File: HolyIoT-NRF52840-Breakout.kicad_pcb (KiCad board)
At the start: 2 copper layers, 45 x 60 mm, 8 parts, among them J1 Conn_01x22_Male, J2 Conn_01x22_Male, J3 Conn_01x11_Male, P1 USB_micro_B, U1 HolyIOT_NRF52840

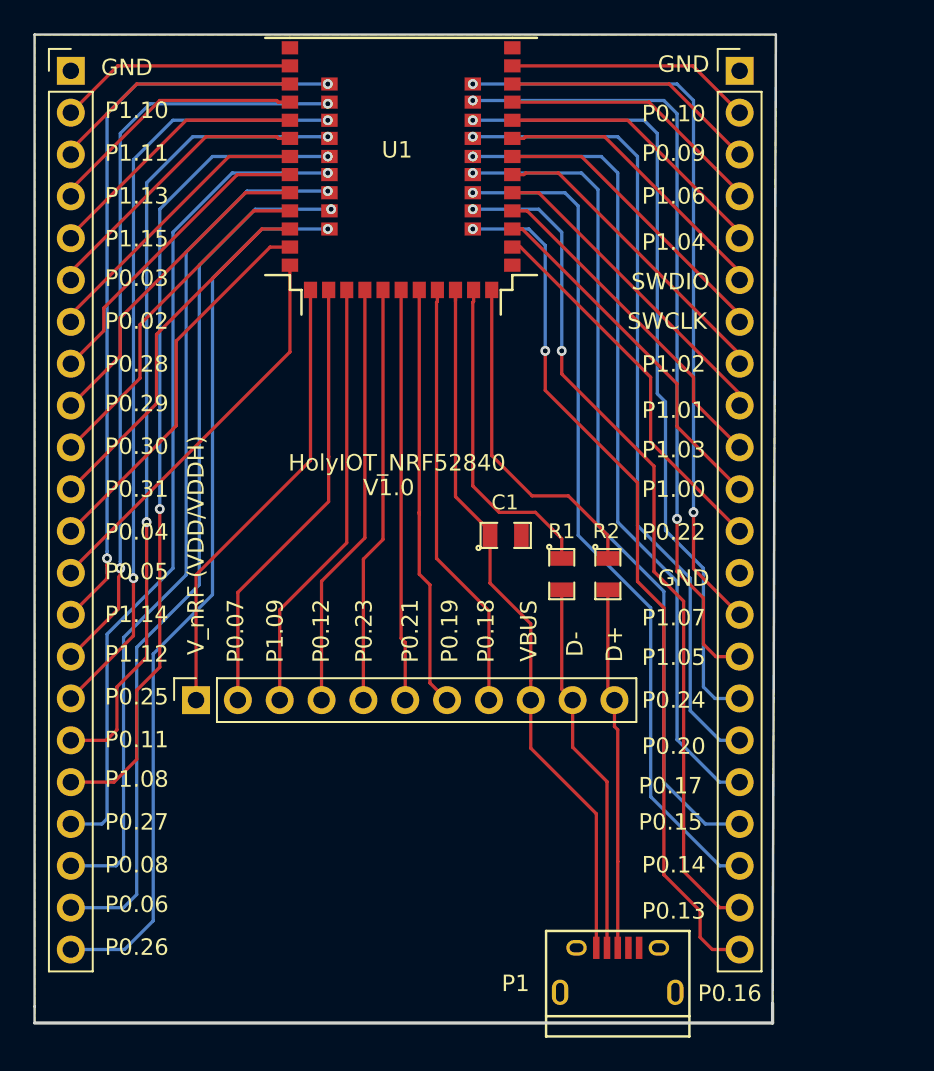
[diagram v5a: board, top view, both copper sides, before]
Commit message: Morning Routing is always the best...
 - Routing DONE in 2 Layers
- Verification has to be done before order...
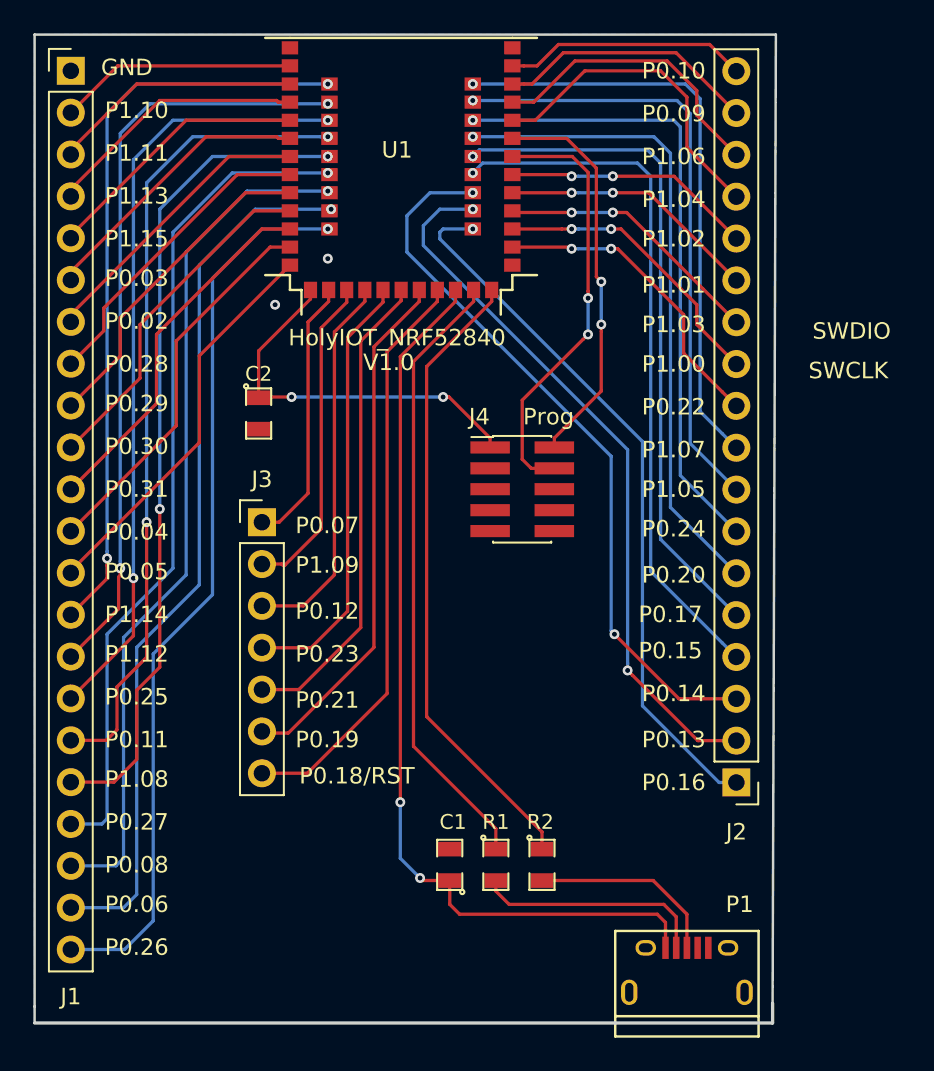
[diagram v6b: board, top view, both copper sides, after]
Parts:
- added C2: C, MWL:SM0805, F.Cu at (109.6, 105.0)
- added J4: Prog, Connector_PinHeader_1.27mm:PinHeader_2x05_P1.27mm_Vertical_SMD, F.Cu at (125.6, 109.6)
- J2: value Conn_01x22_Male -> Conn_01x18_Male; footprint Connector_PinHeader_2.54mm:PinHeader_1x22_P2.54mm_Vertical -> Connector_PinHeader_2.54mm:PinHeader_1x18_P2.54mm_Vertical
- J3: value Conn_01x11_Male -> Conn_01x07_Male; footprint Connector_PinSocket_2.54mm:PinSocket_1x11_P2.54mm_Vertical -> Connector_PinHeader_2.54mm:PinHeader_1x07_P2.54mm_Vertical
- moved J2 43.2 mm to (138.6, 127.4), turned to 180 degrees
- moved C1 20.3 mm to (121.2, 132.4), turned to 90 degrees
- moved R2 18.1 mm to (126.8, 132.4)
- moved R1 18.1 mm to (124.0, 132.4)
- moved J3 11.5 mm to (109.8, 111.6), turned to 0 degrees
- moved P1 4.20 mm to (135.6, 139.0)
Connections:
- J2 pad 1: GND -> Net-(J2-Pad1)
- J2 pad 13: GND -> Net-(J2-Pad13)
- P1 pad 2: Net-(J3-Pad10) -> Net-(P1-Pad2)
- P1 pad 3: Net-(J3-Pad11) -> Net-(P1-Pad3)
- R1 pad 2: Net-(J3-Pad10) -> Net-(P1-Pad2)
- R2 pad 2: Net-(J3-Pad11) -> Net-(P1-Pad3)
- U1 pad 23: Net-(J2-Pad14) -> Net-(J2-Pad9)
- U1 pad 24: Net-(J2-Pad15) -> Net-(J2-Pad8)
- U1 pad 25: Net-(J2-Pad16) -> Net-(J2-Pad7)
- U1 pad 26: Net-(J2-Pad17) -> Net-(J2-Pad6)
- U1 pad 27: Net-(J2-Pad18) -> Net-(J2-Pad5)
- U1 pad 28: Net-(J2-Pad19) -> Net-(J2-Pad4)
- U1 pad 29: Net-(J2-Pad20) -> Net-(J2-Pad3)
- U1 pad 30: Net-(J2-Pad21) -> Net-(J2-Pad2)
- U1 pad 31: Net-(J2-Pad22) -> Net-(J2-Pad1)
- U1 pad 33: Net-(J2-Pad2) -> Net-(J2-Pad18)
- U1 pad 34: Net-(J2-Pad3) -> Net-(J2-Pad17)
- U1 pad 35: Net-(J2-Pad4) -> Net-(J2-Pad16)
- U1 pad 36: Net-(J2-Pad5) -> Net-(J2-Pad15)
- U1 pad 37: Net-(J2-Pad6) -> SWDIO
- U1 pad 38: Net-(J2-Pad7) -> SWDCLK
- U1 pad 39: Net-(J2-Pad8) -> Net-(J2-Pad14)
- U1 pad 40: Net-(J2-Pad9) -> Net-(J2-Pad13)
- U1 pad 41: Net-(J2-Pad10) -> Net-(J2-Pad12)
- U1 pad 43: Net-(J2-Pad12) -> Net-(J2-Pad10)
- U1 pad 48: Net-(J3-Pad8) -> Net-(J3-Pad7)
- U1 pad 49: Net-(J3-Pad7) -> Net-(J3-Pad6)
- U1 pad 50: Net-(J3-Pad6) -> Net-(J3-Pad5)
- U1 pad 51: Net-(J3-Pad5) -> Net-(J3-Pad4)
- U1 pad 52: Net-(J3-Pad4) -> Net-(J3-Pad3)
- U1 pad 53: Net-(J3-Pad3) -> Net-(J3-Pad2)
- U1 pad 54: Net-(J3-Pad2) -> Net-(J3-Pad1)
- U1 pad 55: Net-(J3-Pad1) -> V_NRF
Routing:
- net Net-(J2-Pad22): track 53.4 -> 0.00 mm, vias 2 -> 0
- net Net-(J2-Pad21): track 52.2 -> 0.00 mm, vias 2 -> 0
- net Net-(J2-Pad20): track 51.6 -> 0.00 mm, vias 1 -> 0
- net Net-(J2-Pad19): track 51.3 -> 0.00 mm, vias 1 -> 0
- net Net-(J2-Pad1): track 0.00 -> 43.6 mm, vias 0 -> 1
- net Net-(J2-Pad18): track 50.0 -> 14.8 mm, vias 1 -> 0
- net Net-(J2-Pad17): track 49.2 -> 15.9 mm, vias 1 -> 0
- net Net-(J2-Pad14): track 46.2 -> 15.2 mm
- net Net-(J2-Pad16): track 48.8 -> 17.9 mm, vias 1 -> 0
- net Net-(J2-Pad2): track 15.0 -> 43.9 mm, vias 0 -> 2
- net Net-(J2-Pad3): track 15.6 -> 44.2 mm, vias 0 -> 2
- net Net-(J2-Pad15): track 48.1 -> 19.8 mm, vias 2 -> 0
- net Net-(J2-Pad4): track 16.3 -> 42.7 mm, vias 0 -> 1
- net SWDCLK: track 0.00 -> 26.2 mm, vias 0 -> 2
- net Net-(J3-Pad8): track 26.2 -> 0.00 mm
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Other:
- board text removed: "D+"
- board text removed: "D-"
- board text removed: "P0.18"
- board text removed: "VBUS"
- board text removed: "V_nRF (VDD/VDDH)"

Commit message: Generate Gerber
Generate Gerber
Rework Edge.Cut
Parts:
- added G1: LOGO, MWL:Serigraphie, B.Cu at (113.8, 134.7)
- added G1: LOGO, MWL:Serigraphie, F.Cu at (113.8, 134.7)
- moved J2 0.40 mm to (139.0, 127.4)
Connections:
- J4 pad 10: Net-(J4-Pad10) -> (no net)
- J4 pad 5: Net-(J4-Pad5) -> (no net)
- J4 pad 6: Net-(J4-Pad6) -> (no net)
- J4 pad 7: Net-(J4-Pad7) -> (no net)
- J4 pad 8: Net-(J4-Pad8) -> (no net)
- J4 pad 9: Net-(J4-Pad9) -> (no net)
- P1 pad 4: Net-(P1-Pad4) -> (no net)
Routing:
- net Net-(J2-Pad4): track 42.7 -> 44.2 mm
- net Net-(J2-Pad5): track 41.2 -> 42.7 mm
- net Net-(J2-Pad7): track 38.7 -> 40.1 mm
- net Net-(J2-Pad6): track 39.6 -> 40.9 mm
- net Net-(J2-Pad8): track 37.5 -> 38.8 mm
- net Net-(J2-Pad9): track 36.3 -> 37.6 mm
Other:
- outline, holes or cut-outs redrawn
- board text added: "HolyIOT_NRF52840"
- board text removed: "SWCLK"
- board text removed: "SWDIO"
